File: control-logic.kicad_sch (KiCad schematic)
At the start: 9 parts, among them SW1 Button, U37 AT28C64B, U41 74HCT00

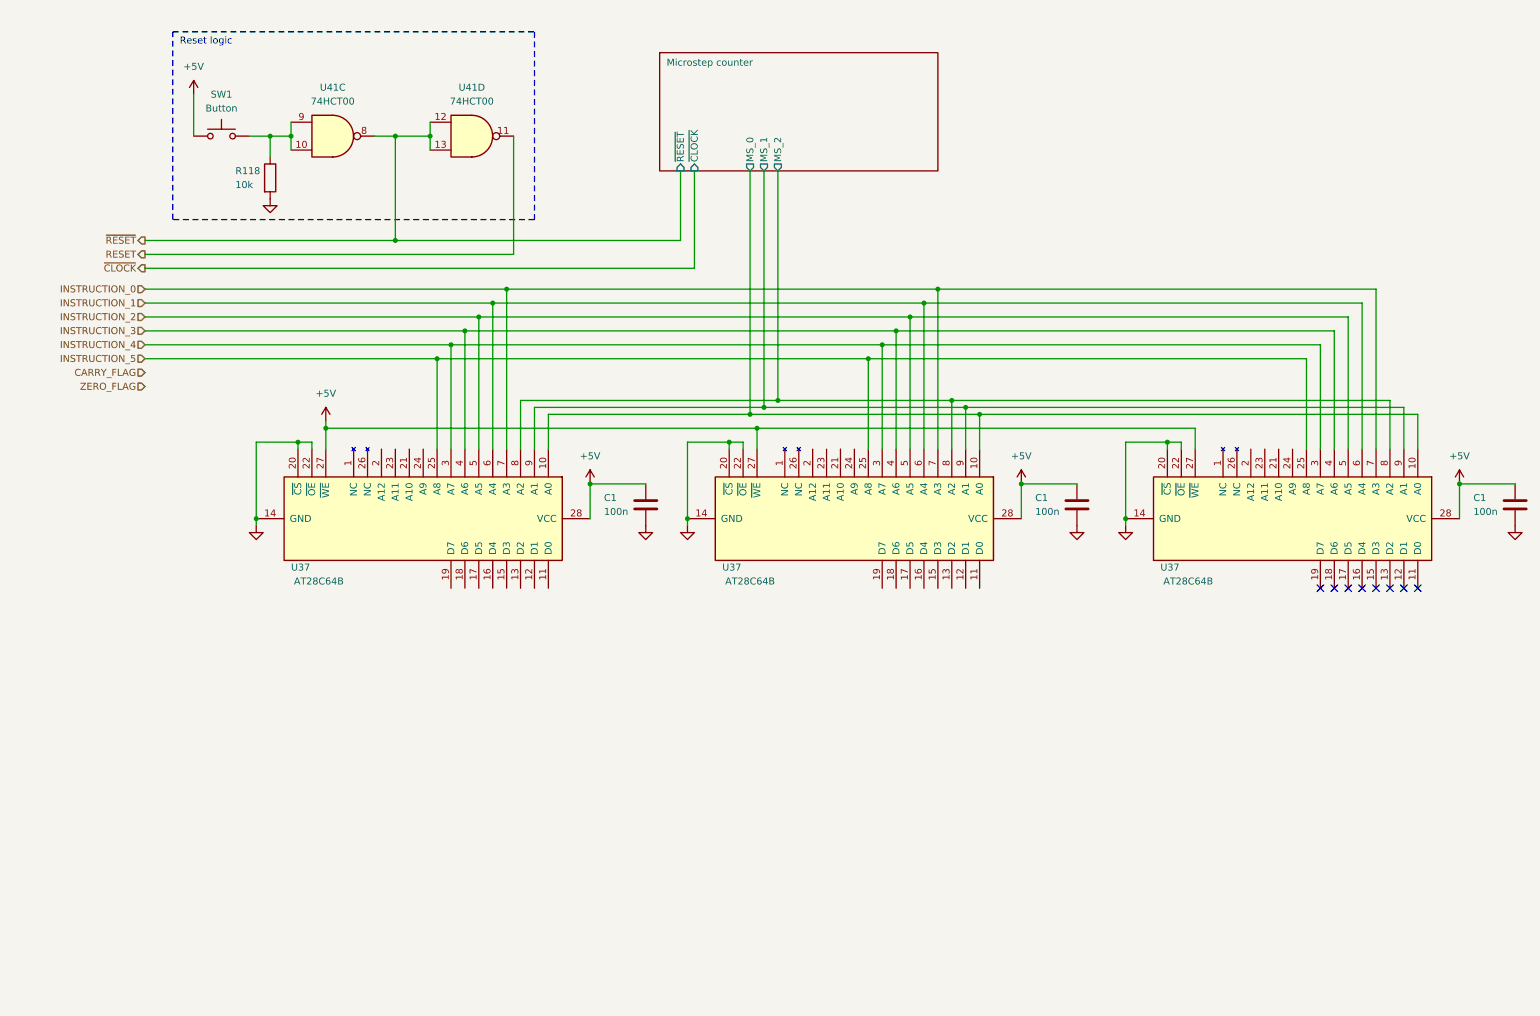
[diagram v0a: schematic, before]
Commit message: finished the control logic
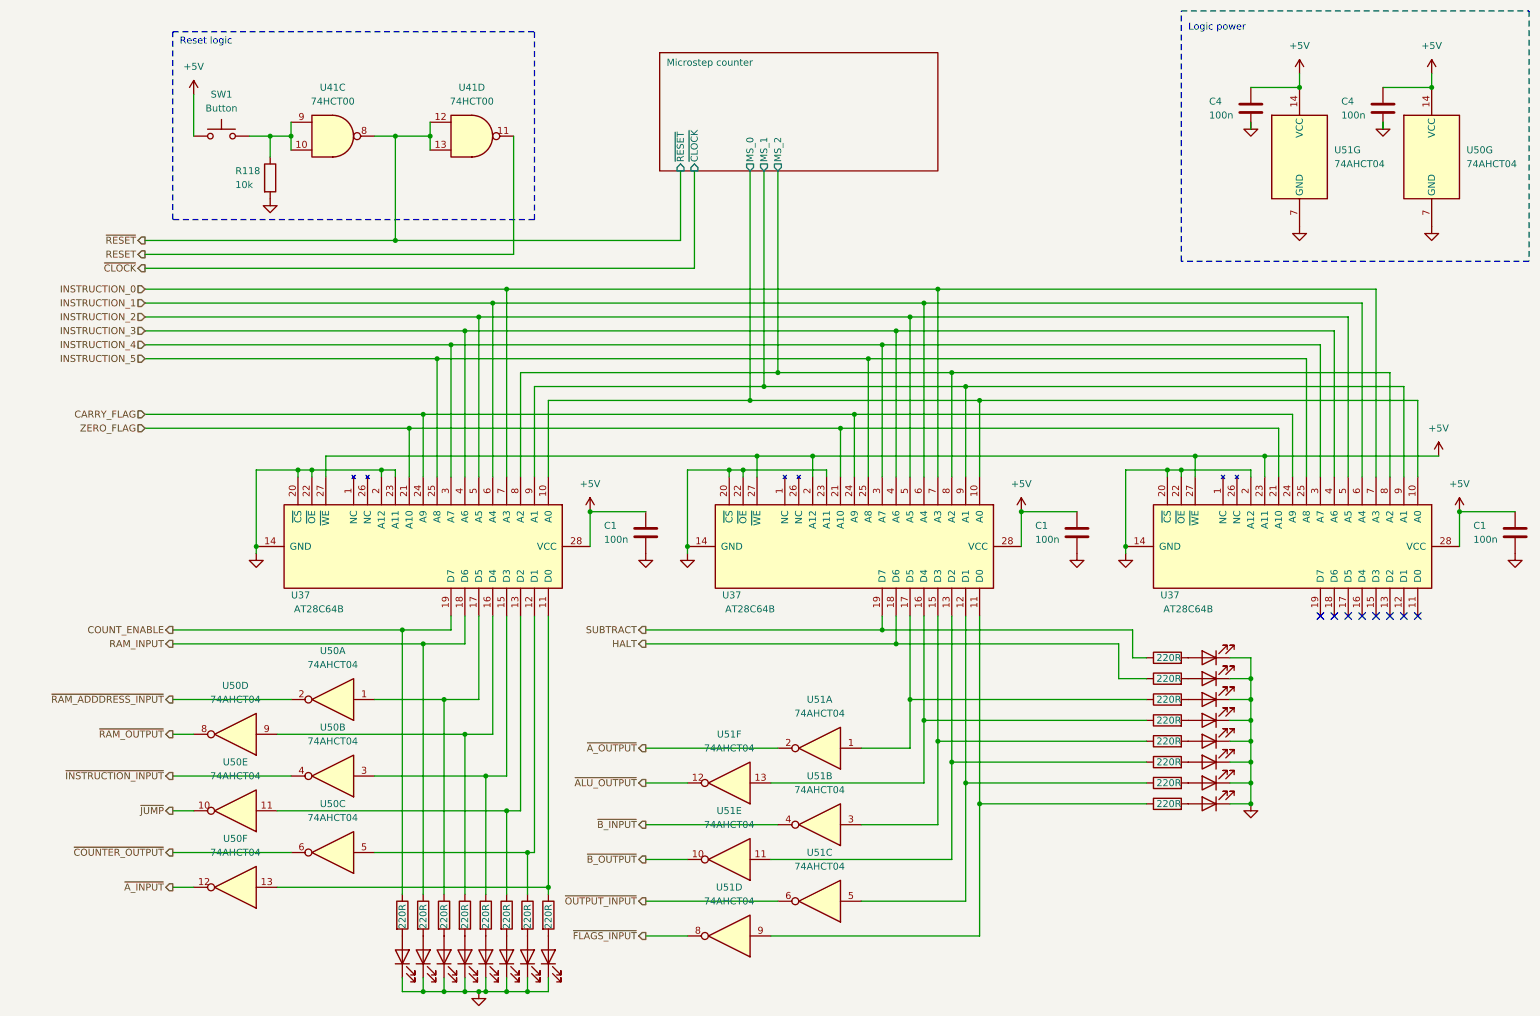
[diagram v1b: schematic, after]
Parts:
- added C4 (x2): 100n, 01_my_library:C_Disc_D4.0mm_W2.6mm_P2.50mm, symbol Device:C
- added D5 (x16): YELLOW, LED_THT:LED_D5.0mm, symbol Device:LED
- added R11 (x16): 220R, Resistor_THT:R_Axial_DIN0204_L3.6mm_D1.6mm_P7.62mm_Horizontal, symbol Device:R
- added U50, U51: 74AHCT04, symbol 74xx:74AHCT04
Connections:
- net +5V: now also U37.2 (A12), U37.23 (A11), C4.1, C4.1, U50.14 (VCC), U51.14 (VCC)
- net CARRY_FLAG: now also U37.24 (A9), U37.24 (A9), U37.24 (A9)
- net GND: now also U37.2 (A12), U37.2 (A12), U37.23 (A11), U37.23 (A11), C4.2, C4.2, D5.1 (K), D5.1 (K), D5.1 (K), D5.1 (K), D5.1 (K), D5.1 (K), D5.1 (K), D5.1 (K), D5.1 (K), D5.1 (K), D5.1 (K), D5.1 (K), D5.1 (K), D5.1 (K), D5.1 (K), D5.1 (K), U50.7 (GND), U51.7 (GND)
- net ZERO_FLAG: now also U37.21 (A10), U37.21 (A10), U37.21 (A10)
- net at U37.11 (D0): now also R11.1, U51.9
- net at U37.12 (D1): now also R11.1, U51.5
- net at U37.13 (D2): now also R11.1, U51.11
- net at U37.15 (D3): now also R11.1, U51.3
- net at U37.16 (D4): now also R11.1, U51.13
- net at U37.17 (D5): now also R11.1, U51.1
- net HALT: now reaches U37.18 (D6)
- net HALT: now also R11.1
- net SUBTRACT: now reaches U37.19 (D7)
- net SUBTRACT: now also R11.1
- net at U37.11 (D0): now also R11.1, U50.13
- net at U37.12 (D1): now also R11.1, U50.5
- net at U37.13 (D2): now also R11.1, U50.11
- net at U37.15 (D3): now also R11.1, U50.3
- net at U37.16 (D4): now also R11.1, U50.9
- net at U37.17 (D5): now also R11.1, U50.1
- net RAM_INPUT: now reaches U37.18 (D6)
- net RAM_INPUT: now also R11.1
- net COUNT_ENABLE: now reaches U37.19 (D7)
- net COUNT_ENABLE: now also R11.1
- new net: D5.2 (A), R11.2 (x16)
- new net ~{ALU_OUTPUT}: U51.12
- new net ~{A_INPUT}: U50.12
- new net ~{A_OUTPUT}: U51.2
- new net ~{B_INPUT}: U51.4
- new net ~{B_OUTPUT}: U51.10
- new net ~{COUNTER_OUTPUT}: U50.6
- new net ~{FLAGS_INPUT}: U51.8
- new net ~{INSTRUCTION_INPUT}: U50.4
- new net ~{JUMP}: U50.10
- new net ~{OUTPUT_INPUT}: U51.6
- new net ~{RAM_ADDDRESS_INPUT}: U50.2
- new net ~{RAM_OUTPUT}: U50.8
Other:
- note added: "Logic power"
- moved on the sheet: C1, U37

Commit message: redid the eeprom
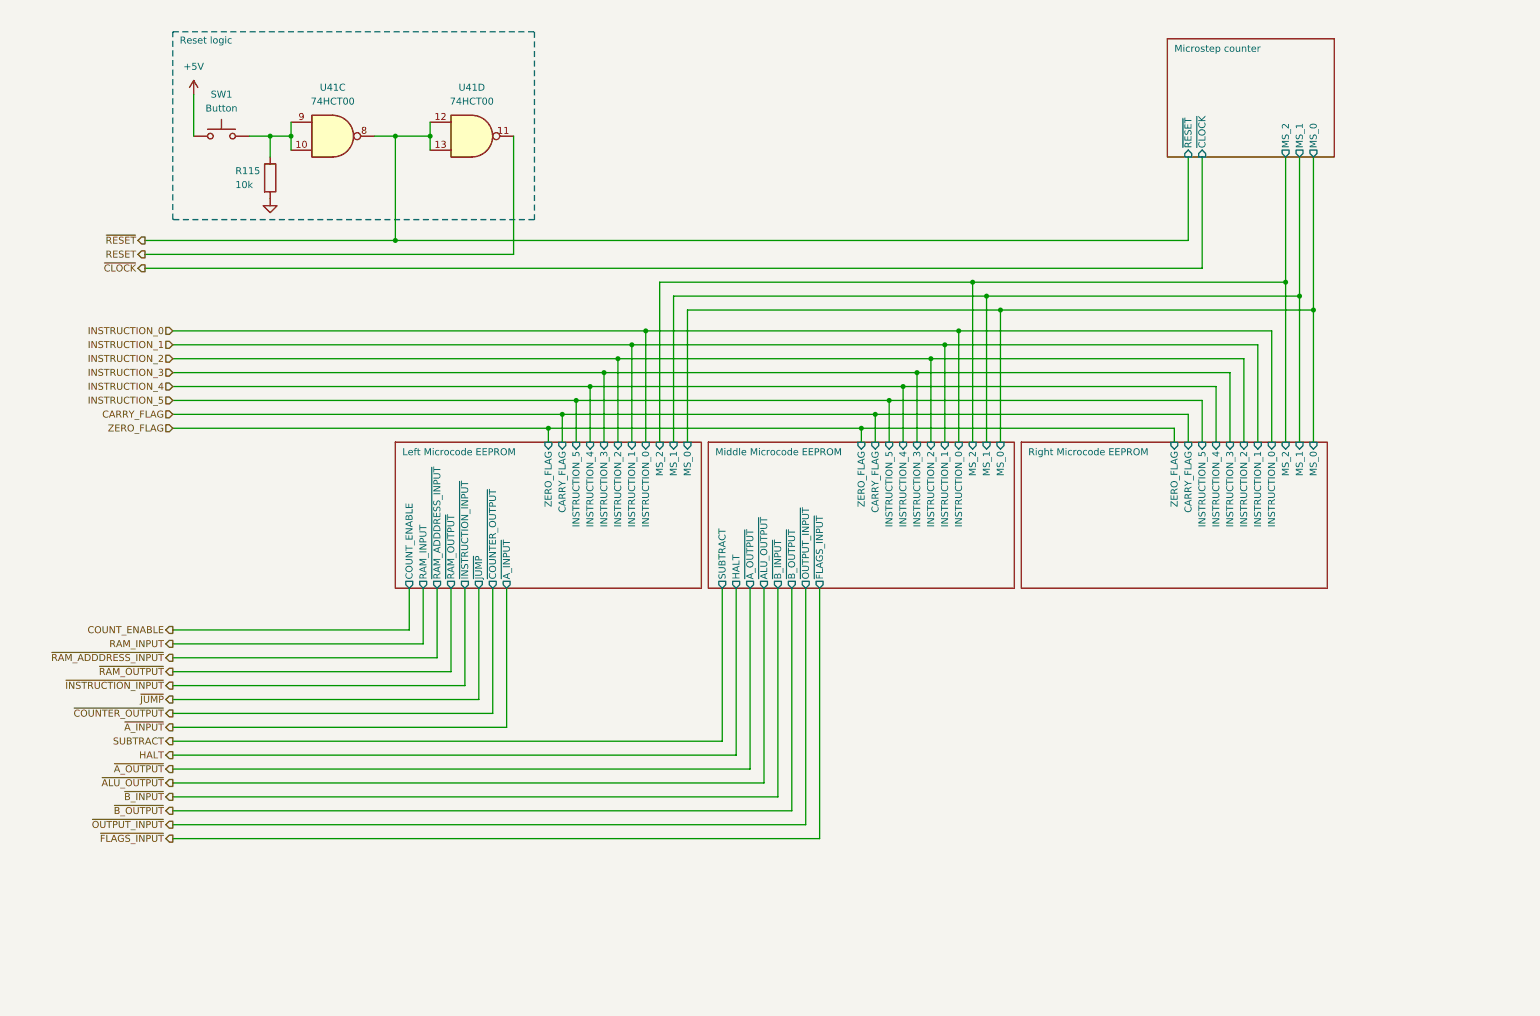
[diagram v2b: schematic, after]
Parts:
- removed C1 (x3), C4 (x2): 100n, 01_my_library:C_Disc_D4.0mm_W2.6mm_P2.50mm, symbol Device:C
- removed D5 (x16): YELLOW, LED_THT:LED_D5.0mm, symbol Device:LED
- removed R11 (x16): 220R, Resistor_THT:R_Axial_DIN0204_L3.6mm_D1.6mm_P7.62mm_Horizontal, symbol Device:R
- removed U37 (x3): AT28C64B, Package_DIP:DIP-28_W15.24mm_Socket, symbol 01_my_library:28C64B
- removed U50, U51: 74AHCT04, symbol 74xx:74AHCT04
- renumbered R118 to R115
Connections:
- no-connect marks 8 -> 0
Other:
- added sheet Left Microcode EEPROM (left-microcode-eeprom.kicad_sch)
- added sheet Middle Microcode EEPROM (middle-microcode-eeprom.kicad_sch)
- added sheet Right Microcode EEPROM (right-microcode-eeprom.kicad_sch)
- note removed: "Logic power"
